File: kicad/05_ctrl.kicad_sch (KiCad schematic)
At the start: 24 parts, among them J501 PG ON_OFF GND, U501 LM393DR, U502 LM393DR, U503 TL431BDBZR, U504 PC817, U505 PC817

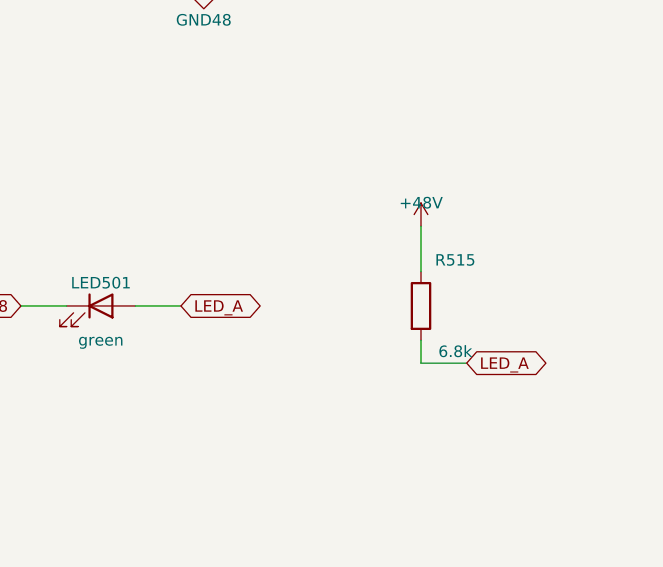
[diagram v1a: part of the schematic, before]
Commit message: Этап 4: генерация PCB (pcbgen: 167 корпусов + 4 отверстия), размещение, DRC без ошибок; правки схемы (SEC_A->AUX_SEC, LED_A->STATUS_LED)
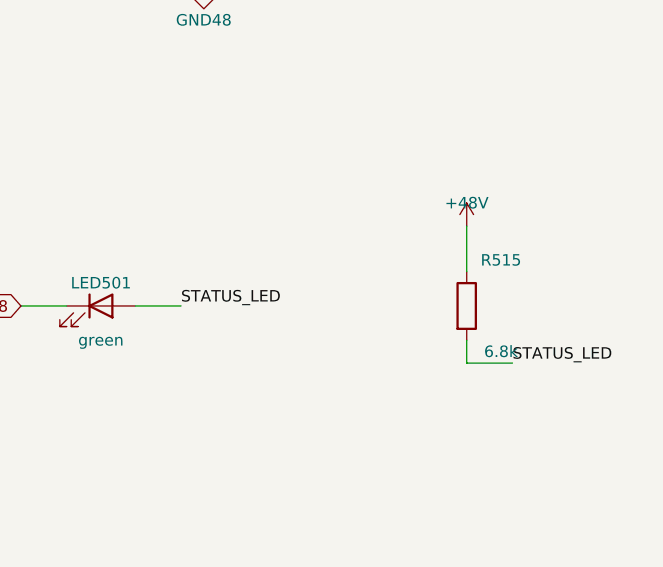
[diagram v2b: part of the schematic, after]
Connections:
- net LED_A renamed STATUS_LED
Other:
- moved on the sheet: R515
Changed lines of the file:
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@@
 		)
 	)
-	(global_label "LED_A"
-		(shape bidirectional)
+	(label "STATUS_LED"
 		(at 318.77 146.05 0)
-		(fields_autoplaced yes)
 		(effects
 			(font
 				(size 1.27 1.27)
 			)
-			(justify left)
+			(justify left bottom)
 		)
 	)
 	(symbol
 		(lib_id "Device:R")
-		(at 345.44 146.05 0)
+		(at 350.52 146.05 0)
 		(unit 1)
 		(exclude_from_sim no)
@@
 		(dnp no)
 		(property "Reference" "R515"
-			(at 349.25 140.97 0)
+			(at 354.33 140.97 0)
 			(effects
 				(font
@@
 		)
 		(property "Value" "6.8k"
-			(at 349.25 151.13 0)
+			(at 354.33 151.13 0)
 			(effects
 				(font
@@
 		)
 		(property "Footprint" "Resistor_SMD:R_0805_2012Metric"
-			(at 345.44 146.05 0)
+			(at 350.52 146.05 0)
 			(effects
 				(font
@@
 		)
 		(property "Datasheet" ""
-			(at 345.44 146.05 0)
+			(at 350.52 146.05 0)
 			(effects
 				(font
@@
 		)
 		(property "Description" ""
-			(at 345.44 146.05 0)
+			(at 350.52 146.05 0)
 			(effects
 				(font
@@
 	(wire
 		(pts
-			(xy 345.44 142.24)
-			(xy 345.44 137.16)
+			(xy 350.52 142.24)
+			(xy 350.52 137.16)
 		)
 		(stroke
@@
 	(symbol
 		(lib_id "power:+48V")
-		(at 345.44 137.16 0)
+		(at 350.52 137.16 0)
 		(unit 1)
 		(exclude_from_sim no)
@@
 		(dnp no)
 		(property "Reference" "#PWR0233"
-			(at 345.44 140.97 0)
+			(at 350.52 140.97 0)
 			(effects
 				(font
@@
 		)
 		(property "Value" "+48V"
-			(at 345.44 134.62 0)
+			(at 350.52 134.62 0)
 			(effects
 				(font
@@
 		)
 		(property "Footprint" ""
-			(at 345.44 137.16 0)
+			(at 350.52 137.16 0)
 			(effects
 				(font
@@
 		)
 		(property "Datasheet" ""
-			(at 345.44 137.16 0)
+			(at 350.52 137.16 0)
 			(effects
 				(font
@@
 		)
 		(property "Description" ""
-			(at 345.44 137.16 0)
+			(at 350.52 137.16 0)
 			(effects
 				(font
@@
 	(wire
 		(pts
-			(xy 345.44 149.86)
-			(xy 345.44 152.4)
+			(xy 350.52 149.86)
+			(xy 350.52 152.4)
 		)
 		(stroke
@@
 	(wire
 		(pts
-			(xy 345.44 152.4)
 			(xy 350.52 152.4)
+			(xy 355.6 152.4)
 		)
 		(stroke
@@
 		)
 	)
-	(global_label "LED_A"
-		(shape bidirectional)
-		(at 350.52 152.4 0)
-		(fields_autoplaced yes)
+	(label "STATUS_LED"
+		(at 355.6 152.4 0)
 		(effects
 			(font
 				(size 1.27 1.27)
 			)
-			(justify left)
+			(justify left bottom)
 		)
 	)
